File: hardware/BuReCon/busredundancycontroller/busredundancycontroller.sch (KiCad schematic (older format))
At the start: 12 parts

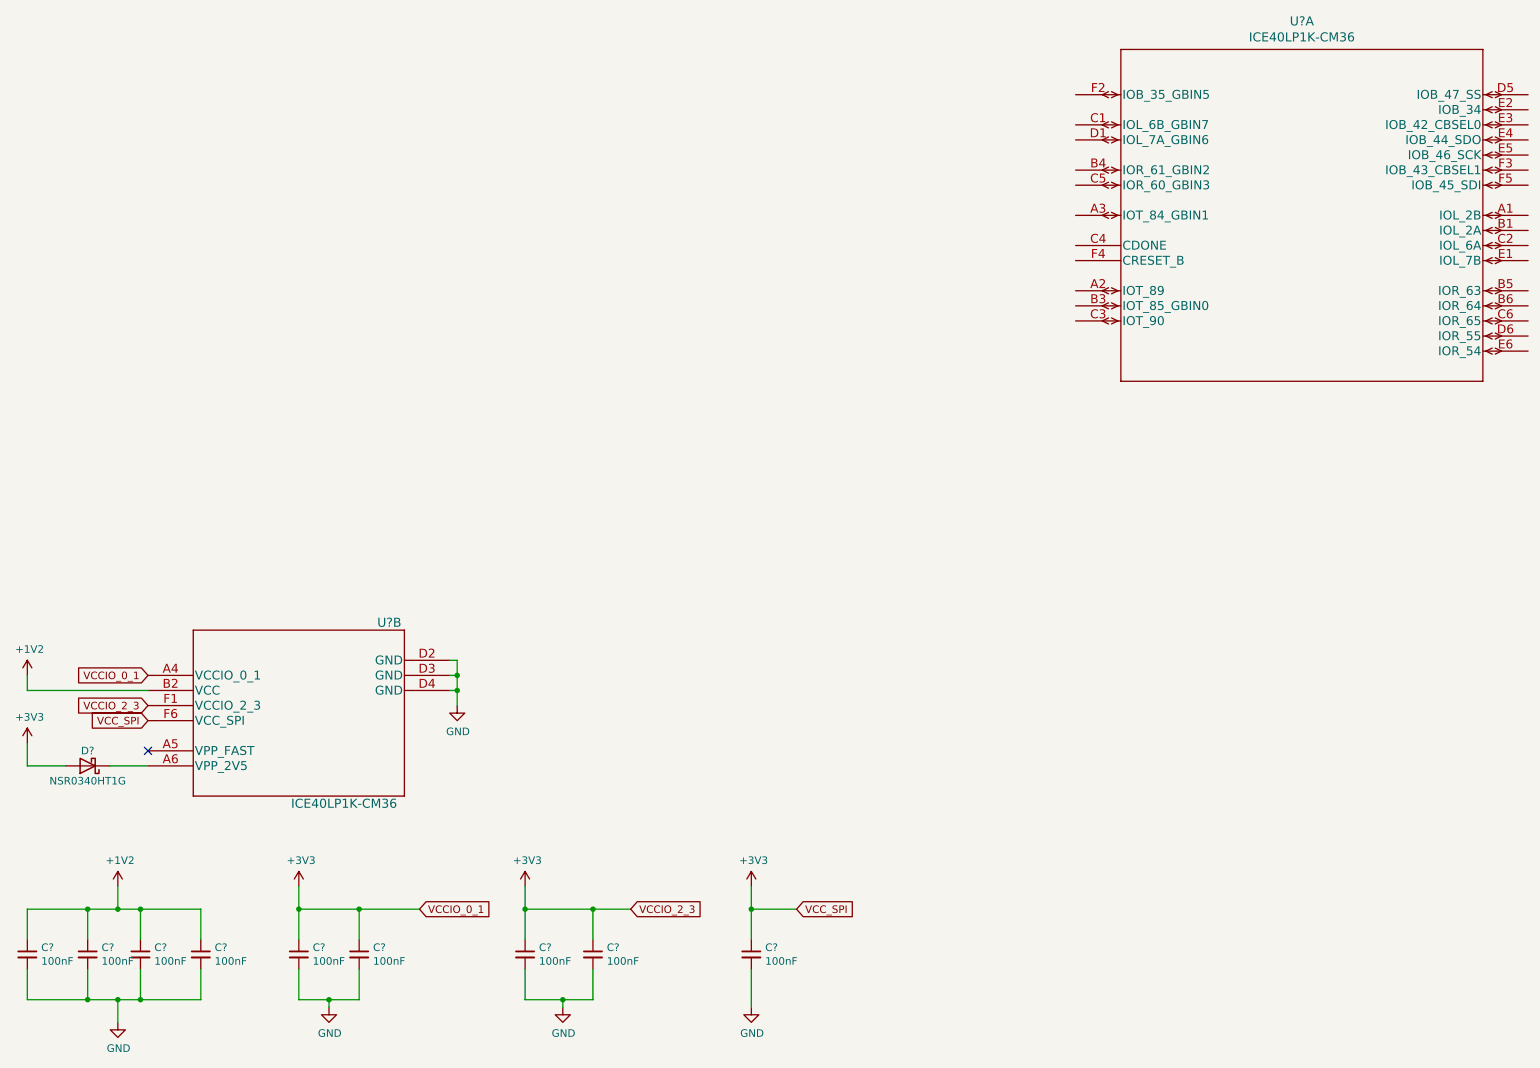
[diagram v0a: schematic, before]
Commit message: Added Power rails and USB
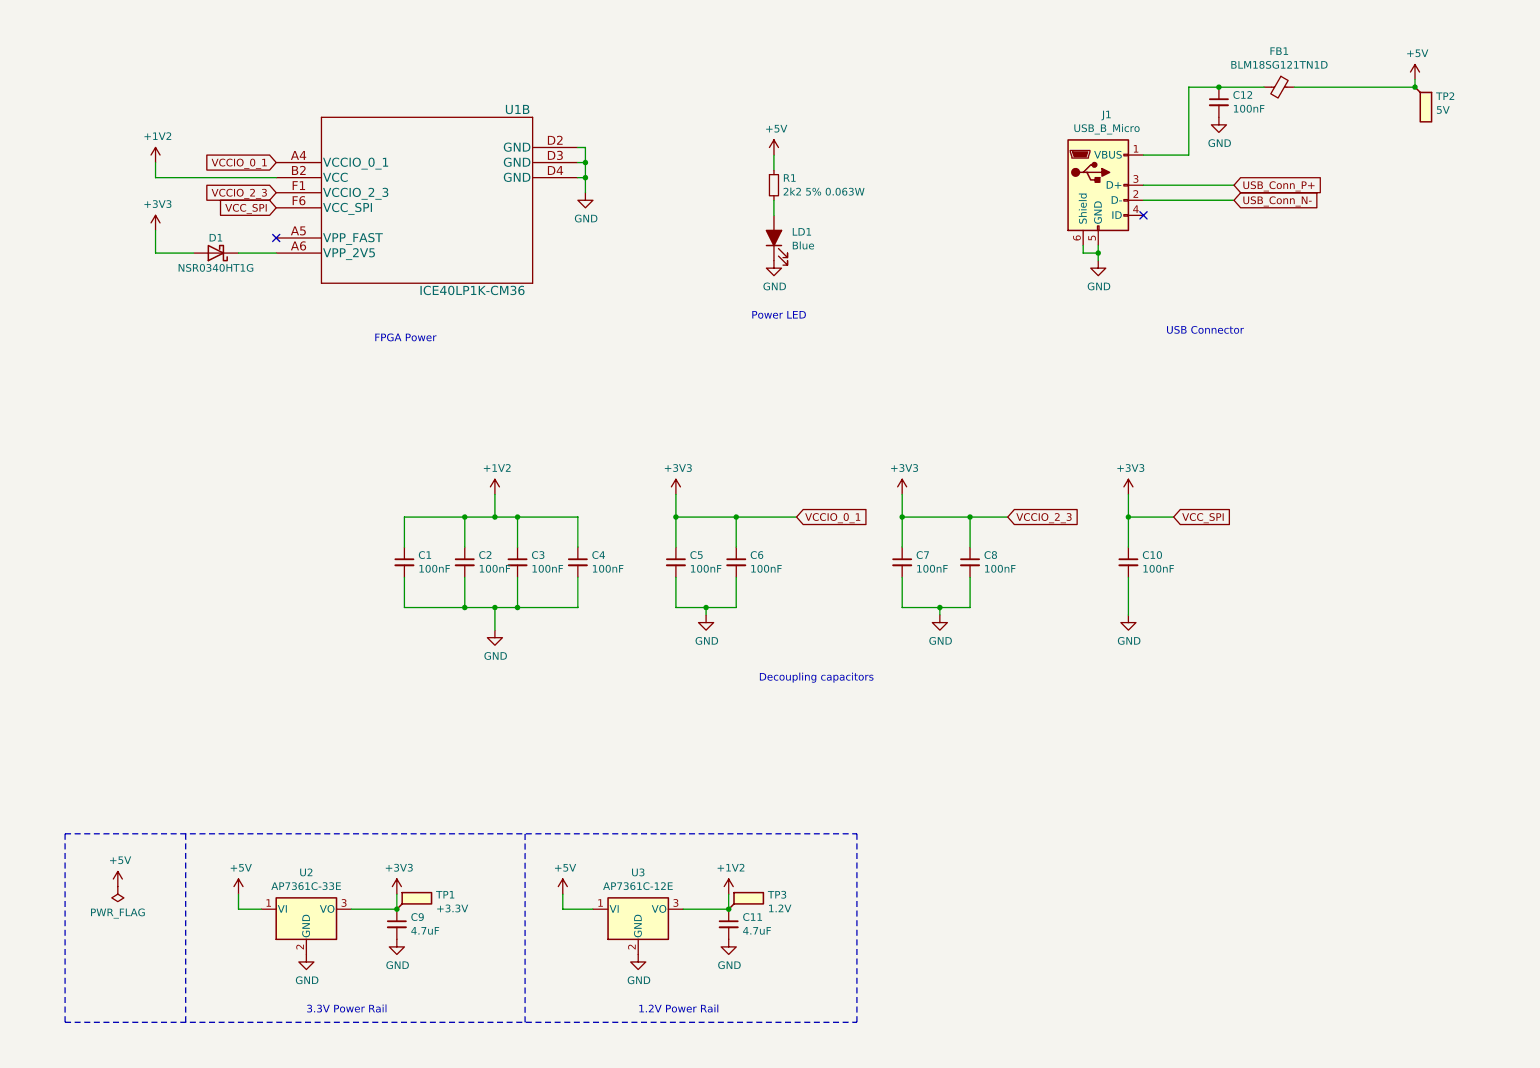
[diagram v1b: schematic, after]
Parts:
- removed U?: ICE40LP1K-CM36, UCBGA36_LAT, symbol ICE40LP1K-CM36:ICE40LP1K-CM36
- added C11, C9: 4.7uF, symbol Device:C_Small
- added C12: 100nF, symbol Device:C_Small
- added FB1: BLM18SG121TN1D, symbol Device:Ferrite_Bead_Small
- added J1: USB_B_Micro, symbol Connector:USB_B_Micro
- added LD1: Blue, symbol Device:LED_ALT
- added R1: 2k2 5% 0.063W, symbol Device:R_Small
- added TP1: +3.3V, symbol Connector:TestPoint_Flag
- added TP2: 5V, symbol Connector:TestPoint_Flag
- added TP3: 1.2V, symbol Connector:TestPoint_Flag
- added U2: AP7361C-33E, Package_TO_SOT_SMD:SOT-223-3_TabPin2, symbol Regulator_Linear:AP7361C-33E
- added U3: AP7361C-12E, Package_TO_SOT_SMD:SOT-223-3_TabPin2, symbol Regulator_Linear:AP7361C-12E
- gave numbers to parts that had none: 11
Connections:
- net +1V2: now also U1.B2 (VCC), C11.1, TP3.1, U3.3 (VO)
- net +3V3: now also U1.A4 (VCCIO_0_1), U1.F1 (VCCIO_2_3), U1.F6 (VCC_SPI), C9.1, TP1.1, U2.3 (VO)
- net GND: now also U1.D2 (GND), U1.D3 (GND), U1.D4 (GND), C11.2, C12.2, C9.2, J1.5 (GND), J1.6 (Shield), LD1.1 (K), U2.2 (GND), U3.2 (GND)
- net at D1.1 (K): now also U1.A6 (VPP_2V5)
- new net: C12.1, FB1.2, J1.1 (VBUS)
- new net: LD1.2 (A), R1.2
- new net +5V: FB1.1, R1.1, TP2.1, U2.1 (VI), U3.1 (VI)
- new net USB_Conn_N-: J1.2 (D-)
- new net USB_Conn_P+: J1.3 (D+)
- no-connect marks 1 -> 2
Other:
- note added: "1.2V Power Rail"
- note added: "3.3V Power Rail"
- note added: "Decoupling capacitors"
- note added: "FPGA Power"
- note added: "Power LED"
- note added: "USB Connector"
- moved on the sheet: C1, C10, C2, C3, C4, C5, C6, C7, C8, D1

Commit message: FT2232 power and ESD
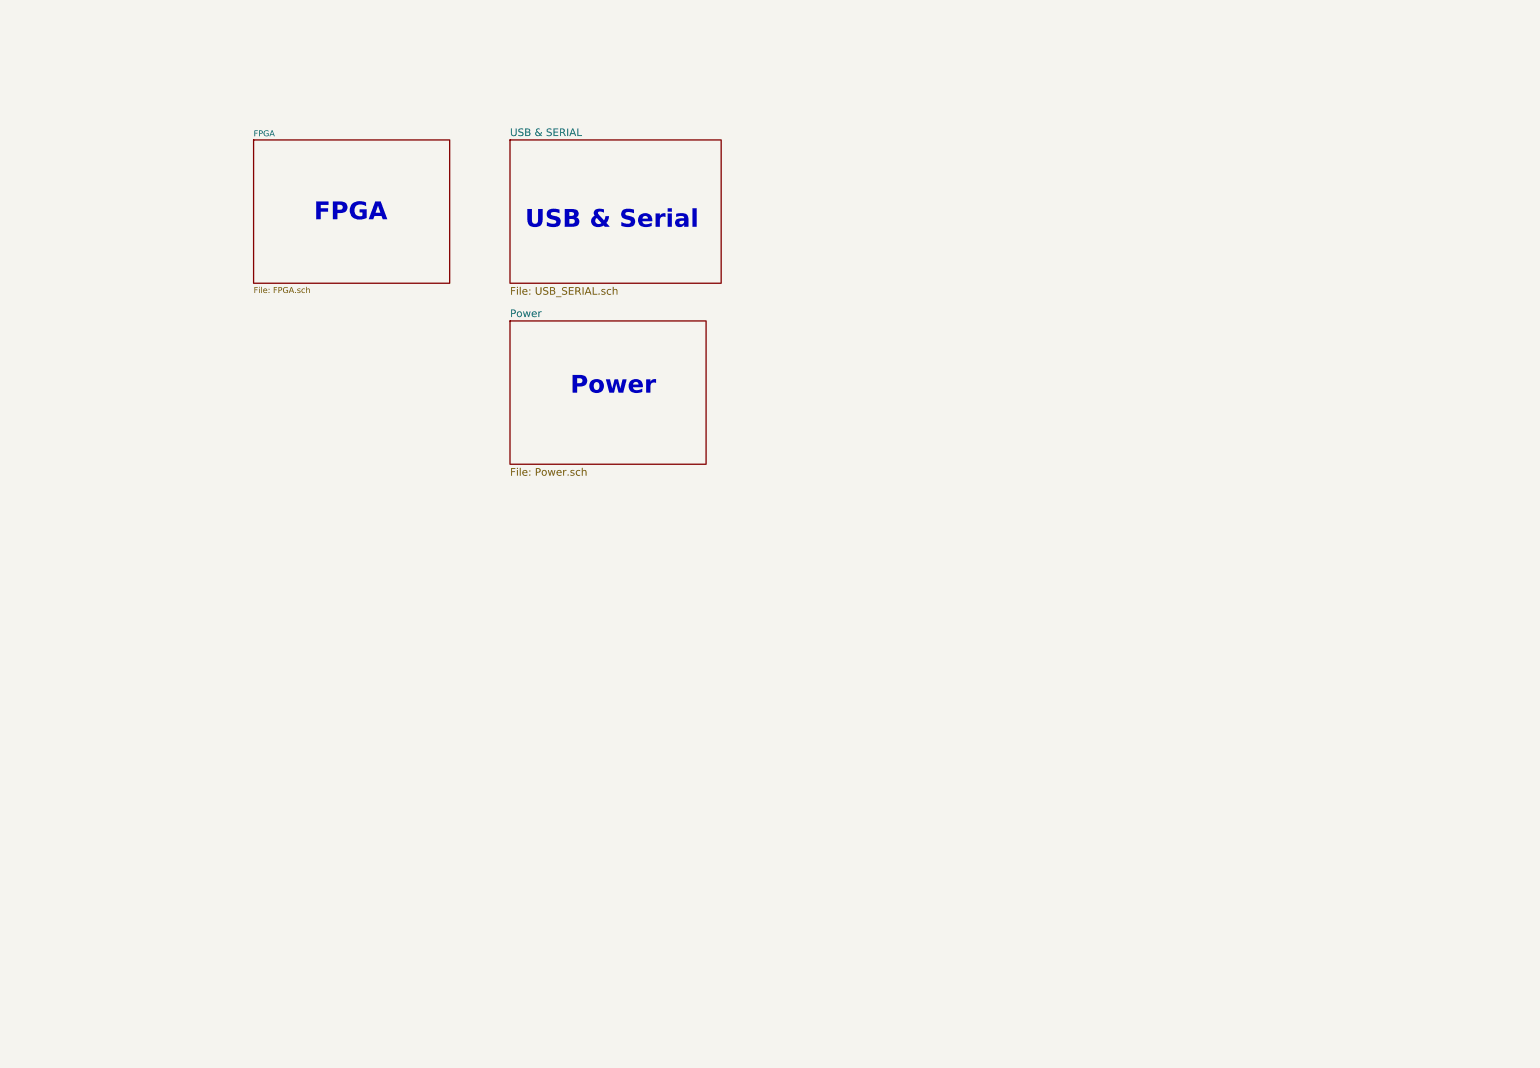
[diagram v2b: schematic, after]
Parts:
- removed C1, C10, C12, C2, C3, C4, C5, C6, C7, C8: 100nF, symbol Device:C_Small
- removed C11, C9: 4.7uF, symbol Device:C_Small
- removed D1: NSR0340HT1G, Diode_SMD:D_SOD-323, symbol Diode:NSR0340HT1G
- removed FB1: BLM18SG121TN1D, symbol Device:Ferrite_Bead_Small
- removed J1: USB_B_Micro, symbol Connector:USB_B_Micro
- removed LD1: Blue, symbol Device:LED_ALT
- removed R1: 2k2 5% 0.063W, symbol Device:R_Small
- removed TP1: +3.3V, symbol Connector:TestPoint_Flag
- removed TP2: 5V, symbol Connector:TestPoint_Flag
- removed TP3: 1.2V, symbol Connector:TestPoint_Flag
- removed U1: ICE40LP1K-CM36, UCBGA36_LAT, symbol ICE40LP1K-CM36:ICE40LP1K-CM36
- removed U2: AP7361C-33E, Package_TO_SOT_SMD:SOT-223-3_TabPin2, symbol Regulator_Linear:AP7361C-33E
- removed U3: AP7361C-12E, Package_TO_SOT_SMD:SOT-223-3_TabPin2, symbol Regulator_Linear:AP7361C-12E
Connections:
- no-connect marks 2 -> 0
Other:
- note added: "FPGA"
- note added: "Power"
- note added: "USB & Serial"
- note removed: "1.2V Power Rail"
- note removed: "3.3V Power Rail"
- note removed: "Decoupling capacitors"
- note removed: "FPGA Power"
- note removed: "Power LED"
- note removed: "USB Connector"

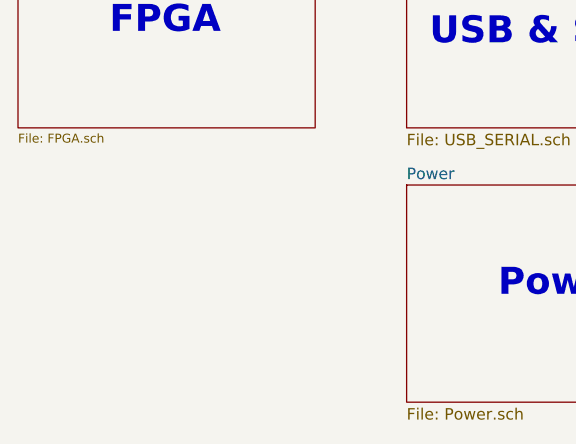
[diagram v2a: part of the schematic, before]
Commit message: FPGA configuration
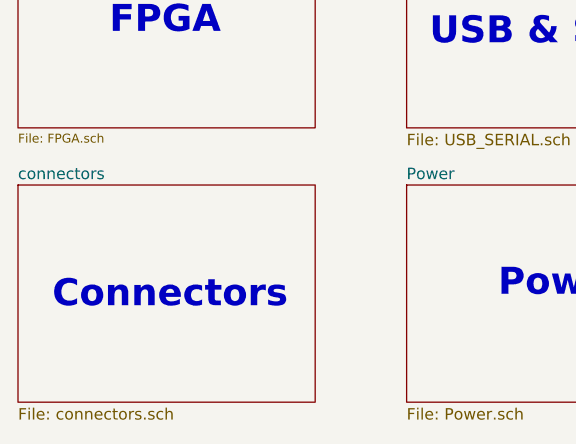
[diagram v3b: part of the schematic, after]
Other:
- note added: "Connectors"
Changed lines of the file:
@@
 $Descr A4 11693 8268
 encoding utf-8
-Sheet 1 4
+Sheet 1 5
 Title "Bus redundancy Controller"
 Date "2020-10-04"
@@
 Text Notes 2650 2100 0    118  ~ 24
 FPGA
+$Sheet
+S 2250 2750 1300 950
+U 5F8745B1
+F0 "connectors" 50
+F1 "connectors.sch" 50
+$EndSheet
+Text Notes 2400 3300 0    118  ~ 24
+Connectors
 $EndSCHEMATC
